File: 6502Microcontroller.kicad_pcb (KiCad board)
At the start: 4 copper layers, 100 x 100 mm, 54 parts, among them IC1 W65C02S6TPG-14, IC2 W65C22S6TPG-14, IC3 AT28HC256E-90SU, IC4 AS6C62256-55PCN, IC5 W65C22S6TPG-14, IC6 W65C51N6TPG-14, IC8 W65C51N6TPG-14, J1 5V GND, J10 Barrel_Jack, J11 Conn_02x02_Counter_Clockwise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

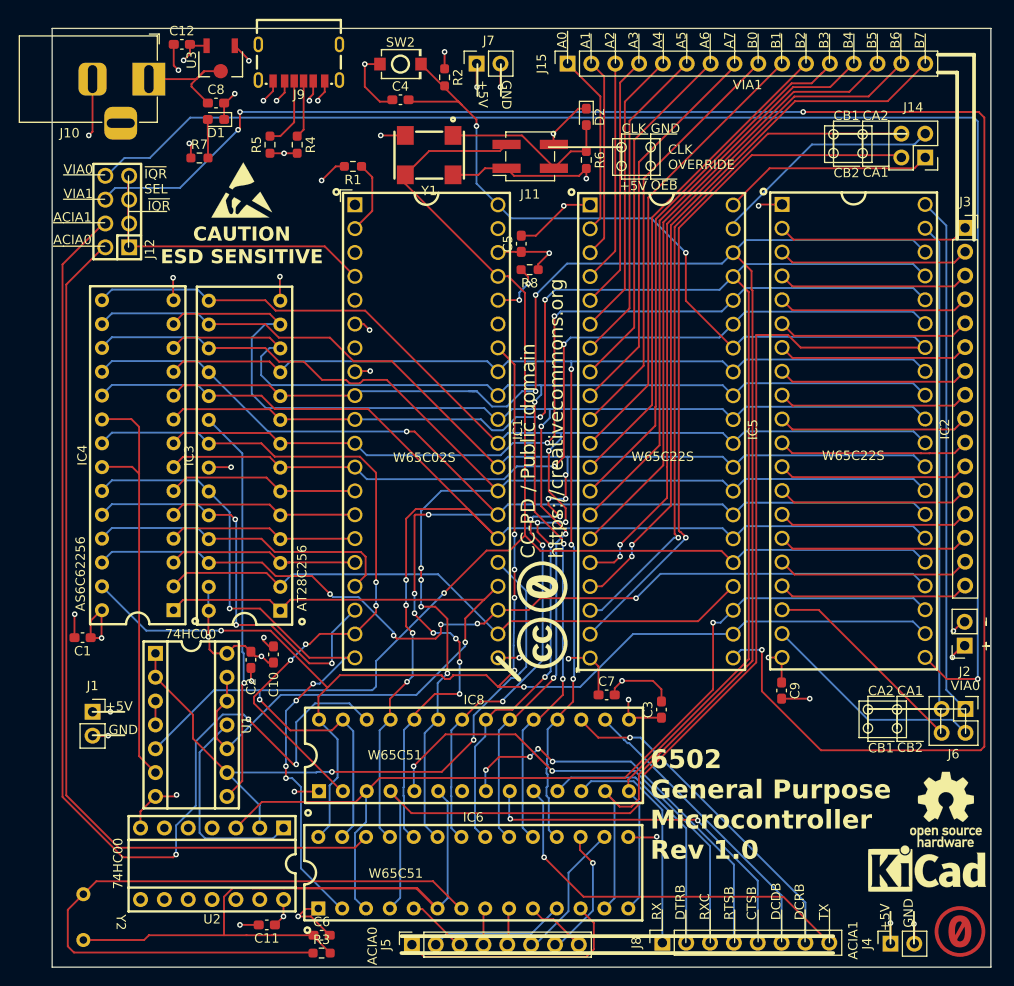
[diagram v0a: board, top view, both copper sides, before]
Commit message: add reset supervisor ic
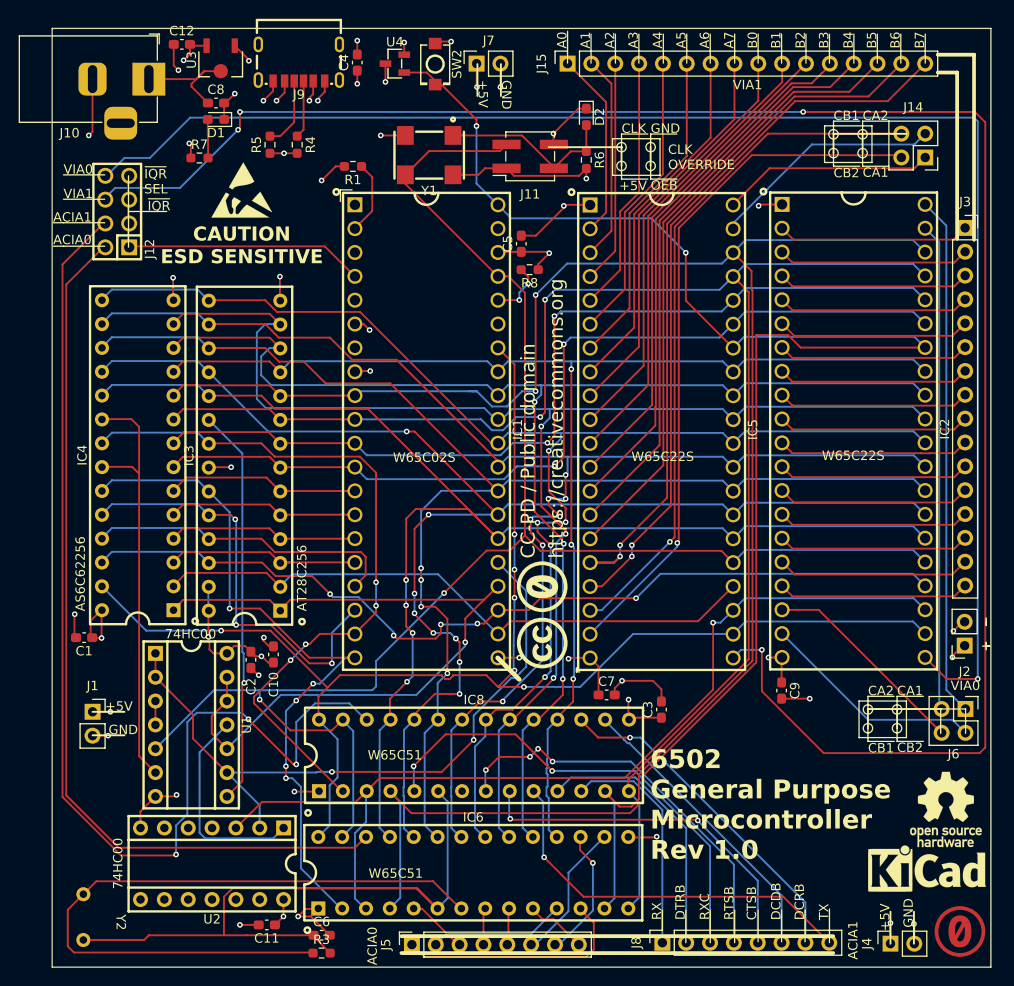
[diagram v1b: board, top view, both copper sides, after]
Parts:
- removed R2: 1k, Resistor_SMD:R_0603_1608Metric_Pad0.98x0.95mm_HandSolder
- added U4: ~, LCSCLib:SOT-23-3_L2.9-W1.3-P1.90-LS2.4-BR, F.Cu at (97.3, 44.0)
- moved C4 6.07 mm to (93.3, 43.9), turned to 90 degrees
- moved SW2 3.70 mm to (101.6, 44.1), turned to -90 degrees
- moved C1 0.16 mm to (64.2, 105.2)
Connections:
- C4 pad 2: ~{RST} -> +5V
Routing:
- net ~{RST}: track 195.1 -> 190.9 mm
- net via1-pb6: track 73.0 -> 76.5 mm
- net GND: track 101.6 -> 98.8 mm, vias 29 -> 31
- net ~{IRQ}_ACIA1: track 118.4 -> 120.2 mm
- net +5V: track 96.7 -> 97.5 mm, vias 22 -> 23
- net d6: track 147.6 -> 146.8 mm
- net via1-cb2: track 74.8 -> 74.2 mm
- net via1-pa1: track 21.3 -> 22.0 mm
- net via1-cb1: track 74.1 -> 73.6 mm

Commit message: feat: add proper headers
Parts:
- J1, J2, J4, J7: footprint Connector_PinSocket_2.54mm:PinSocket_1x02_P2.54mm_Vertical -> LCSCLib:HDR-TH_2P-P2.54-V-F-1
- J11: footprint Connector_PinSocket_2.54mm:PinSocket_2x02_P2.54mm_Vertical_SMD -> LCSCLib:HDR-TH_4P-P2.54-V-F-R2-C2-S2.54
- J14, J6: footprint Connector_PinSocket_2.54mm:PinSocket_2x02_P2.54mm_Vertical -> LCSCLib:HDR-TH_4P-P2.54-V-F-R2-C2-S2.54
- J15, J3: footprint Connector_PinSocket_2.54mm:PinSocket_1x16_P2.54mm_Vertical -> LCSCLib:HDR-TH_16P-P2.54-V-F-4
- J5, J8: footprint Connector_PinSocket_2.54mm:PinSocket_1x08_P2.54mm_Vertical -> LCSCLib:HDR-TH_8P-P2.54-V-F
- moved J15 19.1 mm to (134.8, 44.0), turned to 0 degrees
- moved J3 19.1 mm to (158.1, 80.6), turned to -90 degrees
- moved J8 8.89 mm to (134.7, 137.9), turned to 0 degrees
- moved J5 8.89 mm to (108.0, 137.9), turned to 0 degrees
- moved J6 1.83 mm to (156.8, 114.1), turned to 90 degrees
- moved J14 1.80 mm to (152.5, 52.8)
- moved J7 1.65 mm to (107.5, 43.4), turned to 0 degrees
- moved J1 1.50 mm to (64.2, 114.3), turned to -90 degrees
- moved J4 1.27 mm to (151.4, 137.8), turned to 0 degrees
- moved J2 1.22 mm to (158.0, 104.8), turned to 90 degrees
- moved J11 0.95 mm to (110.8, 53.9)
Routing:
- net via1-cb1: track 73.6 -> 82.1 mm
- net via0-ca2: track 51.9 -> 58.3 mm, vias 0 -> 1
- net via0-ca1: track 55.5 -> 61.4 mm
- net +5V: track 97.5 -> 92.8 mm
- net Net-(D2-A): track 19.3 -> 23.6 mm
- net via1-ca1: track 22.6 -> 24.7 mm
- net GND: track 98.8 -> 97.0 mm, vias 31 -> 32
- net via0-cb1: track 22.4 -> 21.8 mm
- net via0-cb2: track 23.9 -> 24.6 mm
- net ~{RST}: track 190.9 -> 190.2 mm
- net Net-(U3-VIN): track 12.7 -> 13.2 mm
